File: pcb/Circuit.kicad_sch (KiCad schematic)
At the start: 50 parts, among them J1 DTM13-12PA-R008, J2 TSW-101-07-T-D, J3 TSW-101-07-T-D, U1 MCP1700-1802E_TO92, U2 CDP68HC68S1, U3 LM2672N-5.0, U4 Teensy4.0, U5 MCP2562-H-P

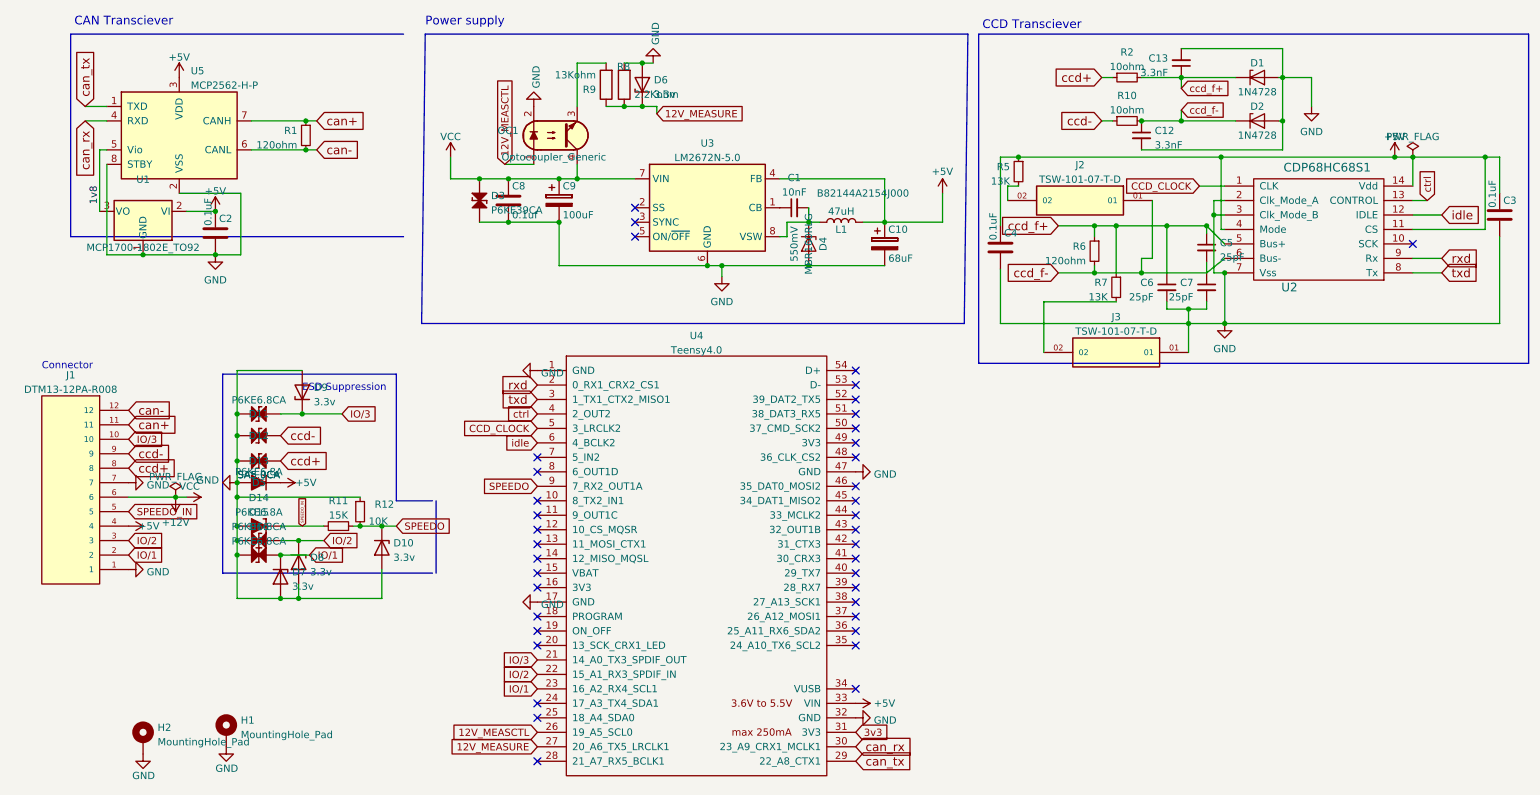
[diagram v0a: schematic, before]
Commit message: Undo attempt to simplify jumpers
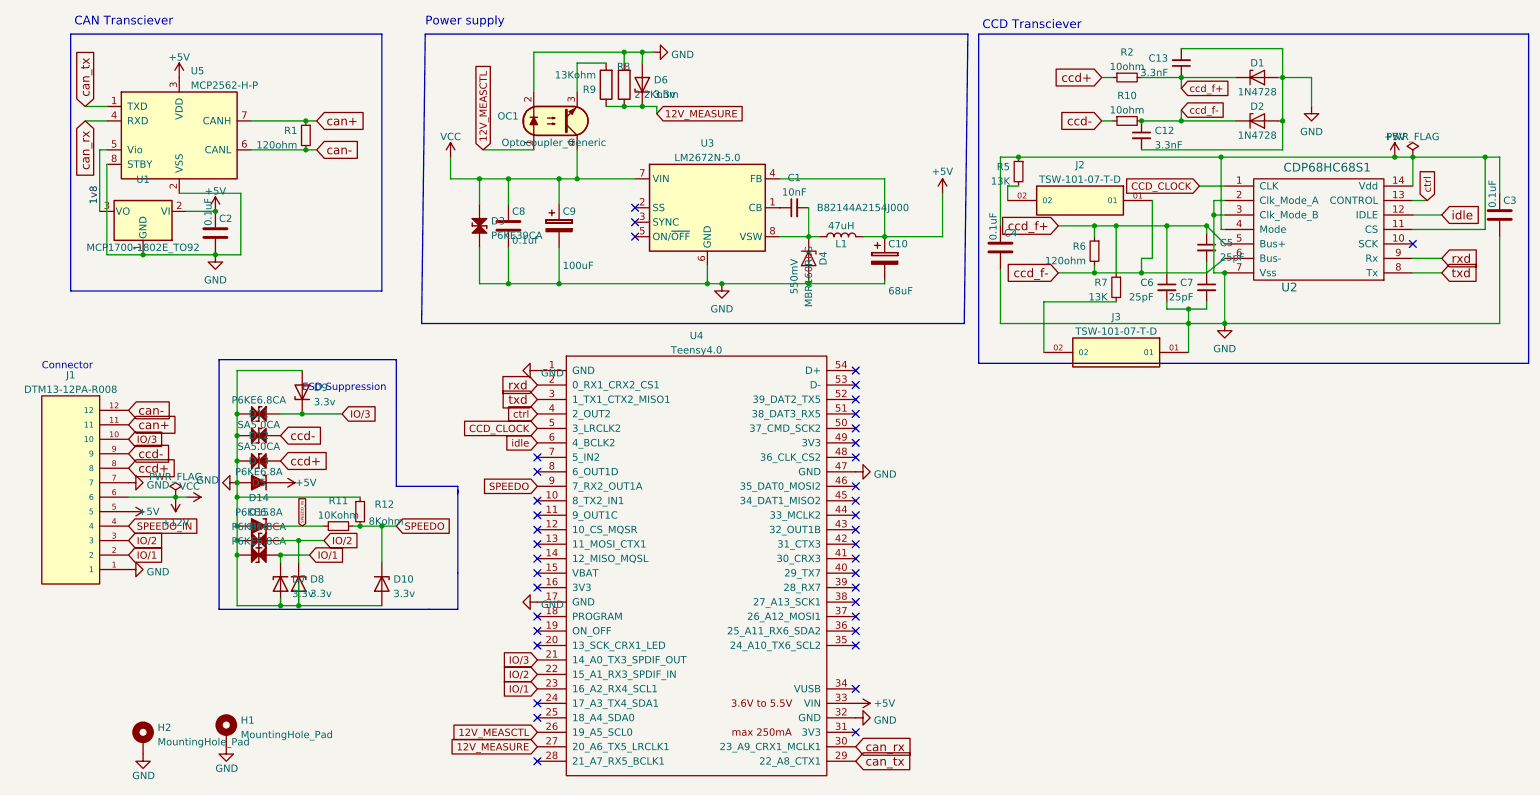
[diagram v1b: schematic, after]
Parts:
- R11: value 15K -> 10Kohm
- R12: value 10K -> 8Kohm
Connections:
- net +5V: now also J1.5; no longer J1.4
- net SPEEDO_IN: now also J1.4; no longer J1.5
- net 3v3: no longer names the net of U4.31 (3V3)
- no-connect marks 39 -> 40
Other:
- company: (none) -> N9 Works
- title: (none) -> XJ/TJ CCD/CAN bus arbiter
- moved on the sheet: C10, C8, C9, D10, D3, D4, D7, D8, L1, OC1
